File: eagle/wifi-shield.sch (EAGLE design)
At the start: 13 parts, among them U1 USB-A-FEMALE

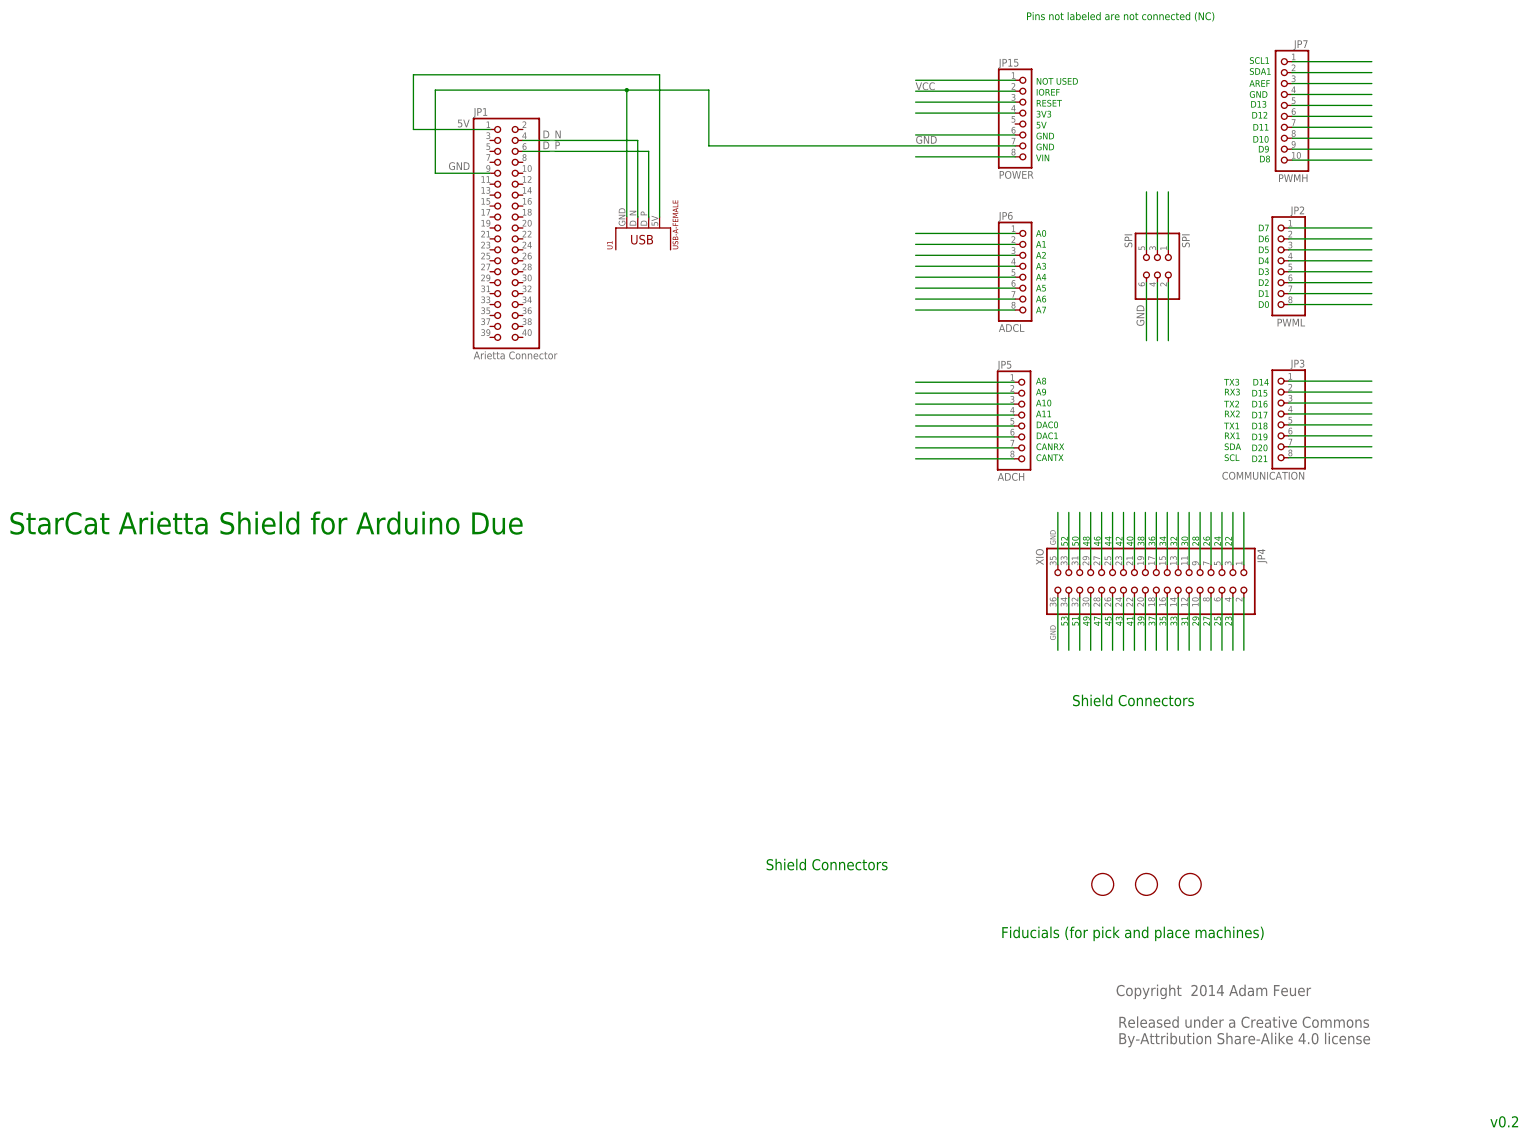
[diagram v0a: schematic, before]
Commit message: added Arietta expansion connector
- to schematic, but not routed yet
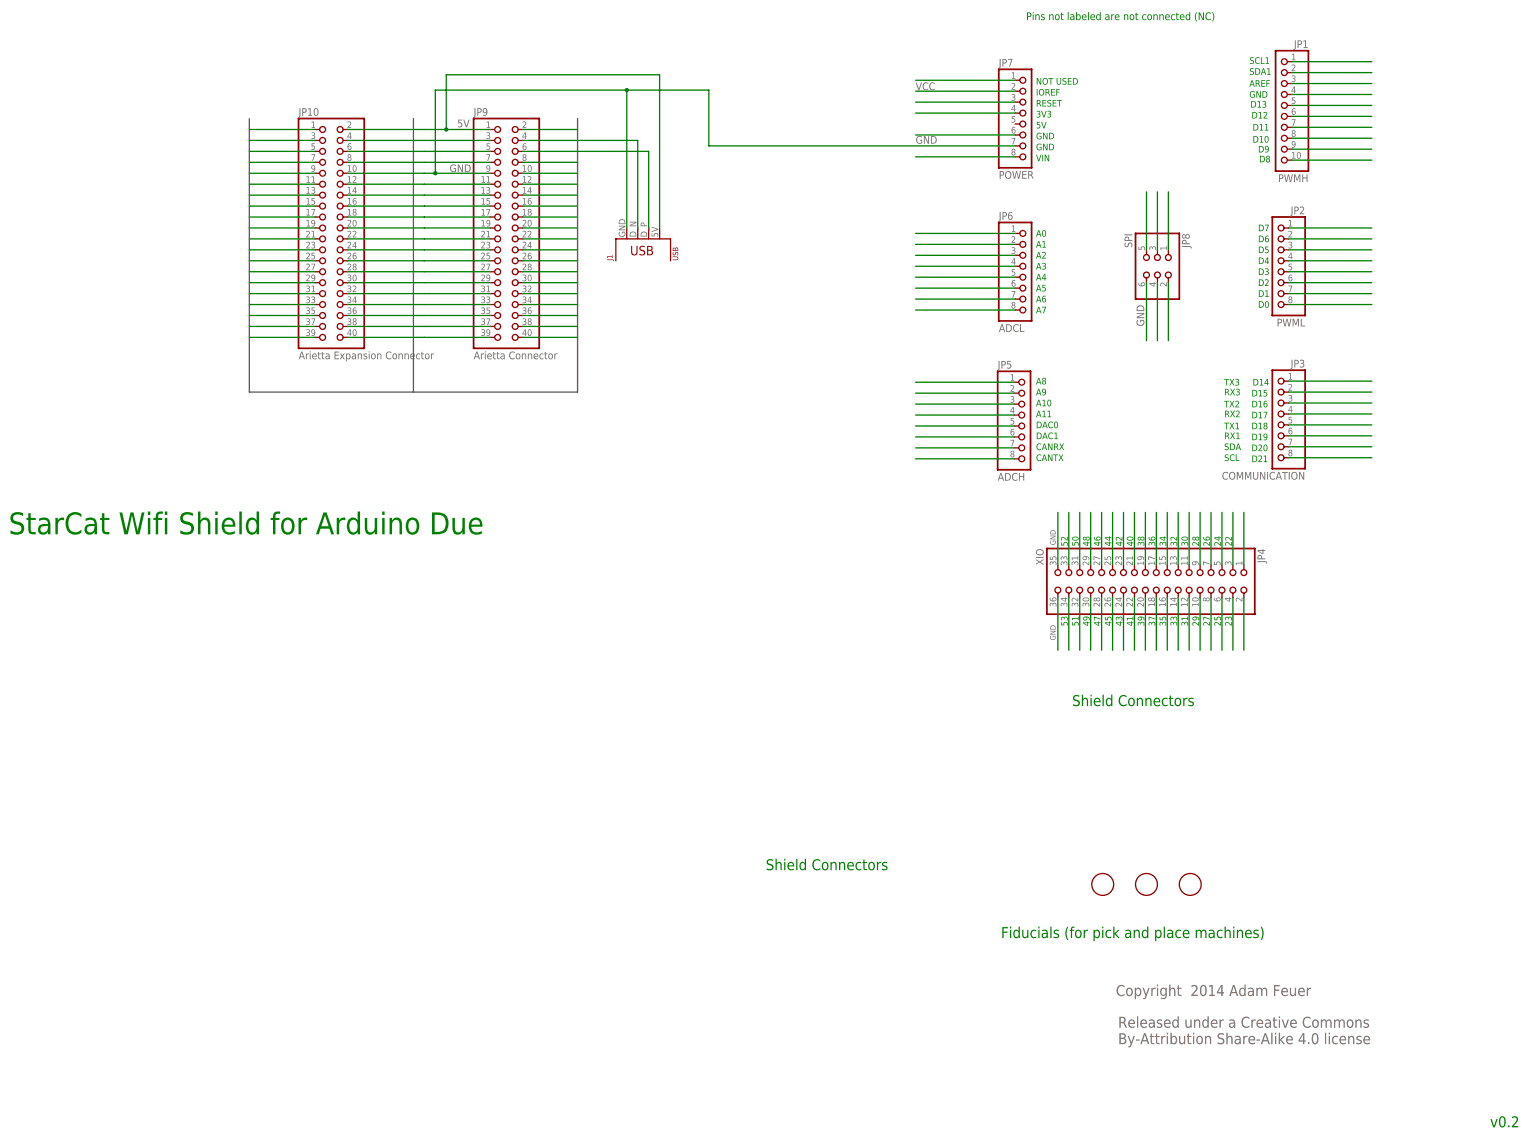
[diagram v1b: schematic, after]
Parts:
- removed JP15: POWER, SmartPrj:PINHD-1X8
- removed U1: USB-A-FEMALE, te-conn-usb:USB-A-FEMALE
- added J1: USB, te-conn-usb:USB-A-FEMALEUSB-A-RIGHT-ANGLE
- added JP10: Arietta Expansion Connector, adafruit:PINHD-2X20
- added JP9: Arietta Connector, adafruit:PINHD-2X20
- JP1: value Arietta Connector -> PWMH; device adafruit:PINHD-2X20 -> SmartPrj:PINHD-1X10
- JP7: value PWMH -> POWER; device SmartPrj:PINHD-1X10 -> SmartPrj:PINHD-1X8
- renumbered SPI to JP8
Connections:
- net D41 renamed N$41
- net D42 renamed N$42
- net D44 renamed N$44A
- removed net N$3 (its old number): JP15.1
- removed net N$571 (its old number): JP15.4
- removed net N$69 (its old number): JP15.8
- removed net N$71 (its old number): JP15.6
- removed net N$72 (its old number): JP15.3
- new net D1: JP10.1
- new net D10: JP10.10, JP9.10
- new net D11: JP10.11, JP9.11
- new net D12: JP10.12, JP9.12
- new net D13: JP10.13, JP9.13
- new net D14: JP10.14, JP9.14
- new net D15: JP10.15, JP9.15
- new net D16: JP10.16, JP9.16
- new net D17: JP10.17, JP9.17
- new net D18: JP10.18, JP9.18
- new net D19: JP10.19, JP9.19
- new net D2: JP10.2, JP9.2
- new net D20: JP10.20, JP9.20
- new net D21: JP10.21, JP9.21
- new net D22: JP10.22, JP9.22
- new net D23: JP10.23, JP9.23
- new net D24: JP10.24, JP9.24
- new net D25: JP10.25, JP9.25
- new net D26: JP10.26, JP9.26
- new net D27: JP10.27, JP9.27
- new net D28: JP10.28, JP9.28
- new net D29: JP10.29, JP9.29
- new net D3: JP10.3, JP9.3
- new net D30: JP10.30, JP9.30
- new net D31: JP10.31, JP9.31
- new net D32: JP10.32, JP9.32
- new net D33: JP10.33, JP9.33
- new net D34: JP10.34, JP9.34
- new net D35: JP10.35, JP9.35
- new net D36: JP10.36, JP9.36
- new net D37: JP10.37, JP9.37
- new net D5: JP10.5, JP9.5
- new net D7: JP10.7, JP9.7
- new net D8: JP10.8, JP9.8
- new net D9: JP10.9
- new net N$10: JP1.6
- new net N$38: JP4.19
- new net N$39: JP4.20
- new net N$40: JP4.21
- new net N$574: JP1.1
- new net N$576: JP1.8
- new net N$7: JP1.3
- new net N$8: JP1.4
- net 5V: now also J1.5V, JP9.1; no longer JP1.1, U1.5V
- net D38: now also JP10.38, JP9.38; no longer JP4.19
- net D39: now also JP10.39, JP9.39; no longer JP4.20
- net D40: now also JP10.40, JP9.40; no longer JP4.21
- net D_N: now also J1.D_N, JP10.4, JP9.4; no longer JP1.4, U1.D_N
- net D_P: now also J1.D_P, JP10.6, JP9.6; no longer JP1.6, U1.D_P
- net GND: now also J1.GND, JP7.7, JP9.9; no longer JP1.9, JP15.7, U1.GND
- net N$1: now also JP1.9; no longer JP7.9
- net N$11: now also JP1.7; no longer JP7.7
- net N$12: now also JP1.10; no longer JP7.10
- net N$575: now also JP1.2; no longer JP7.2
- net N$9: now also JP1.5; no longer JP7.5
- net VCC: now also JP7.2; no longer JP15.2
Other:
- note added: "StarCat Wifi Shield for Arduino Due"
- note removed: "StarCat Arietta Shield for Arduino Due"

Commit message: corrected and routed Arietta auxiliary connector
- net classes are correct
- ERC and DRC pass
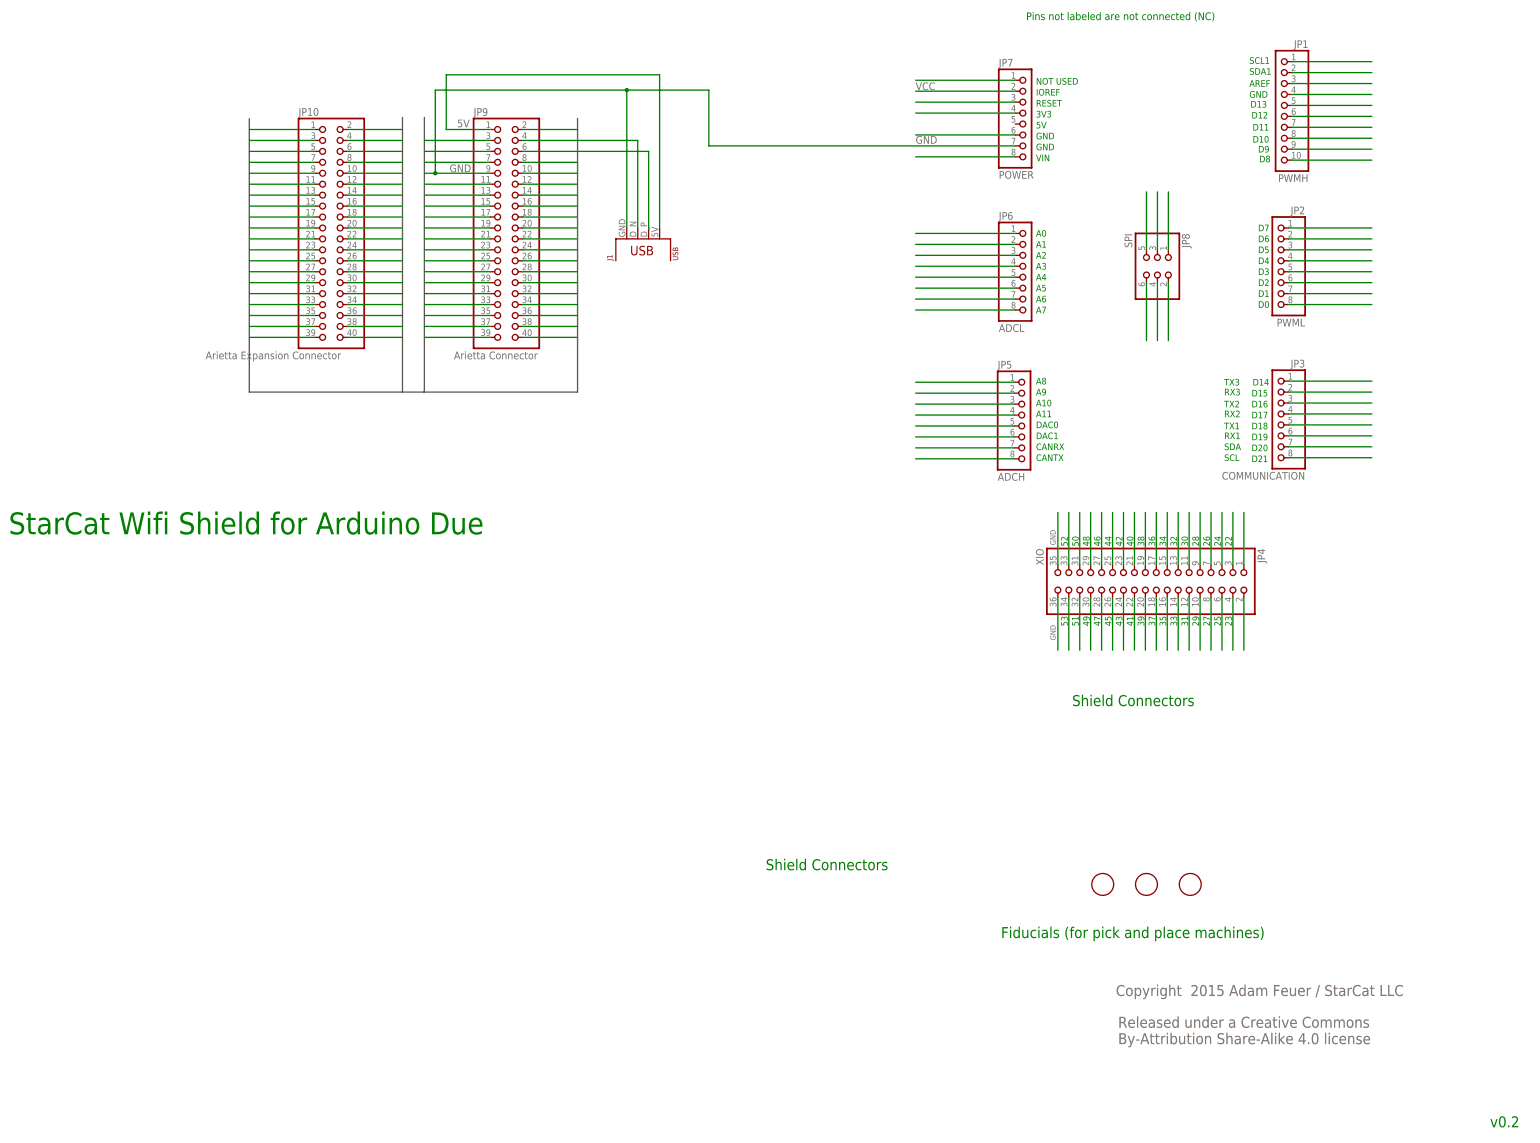
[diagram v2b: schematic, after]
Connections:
- removed net D1: JP10.1
- removed net D9: JP10.9
- new net GND1: JP8.6
- net 5V: now also JP10.1
- net GND: now also JP10.9; no longer JP8.6
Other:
- note added: "Copyright 2015 Adam Feuer / StarCat LLC"
- note removed: "Copyright 2014 Adam Feuer"
